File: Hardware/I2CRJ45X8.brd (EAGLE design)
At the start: 76 x 50 mm, 65 parts, among them IC1 MCP23017SO, IC2 MCP23017SO, J1 I2C-BREAKOUT, J2 I2C-BREAKOUT, J3 M01-PLAIN, J4 RJ45-X8

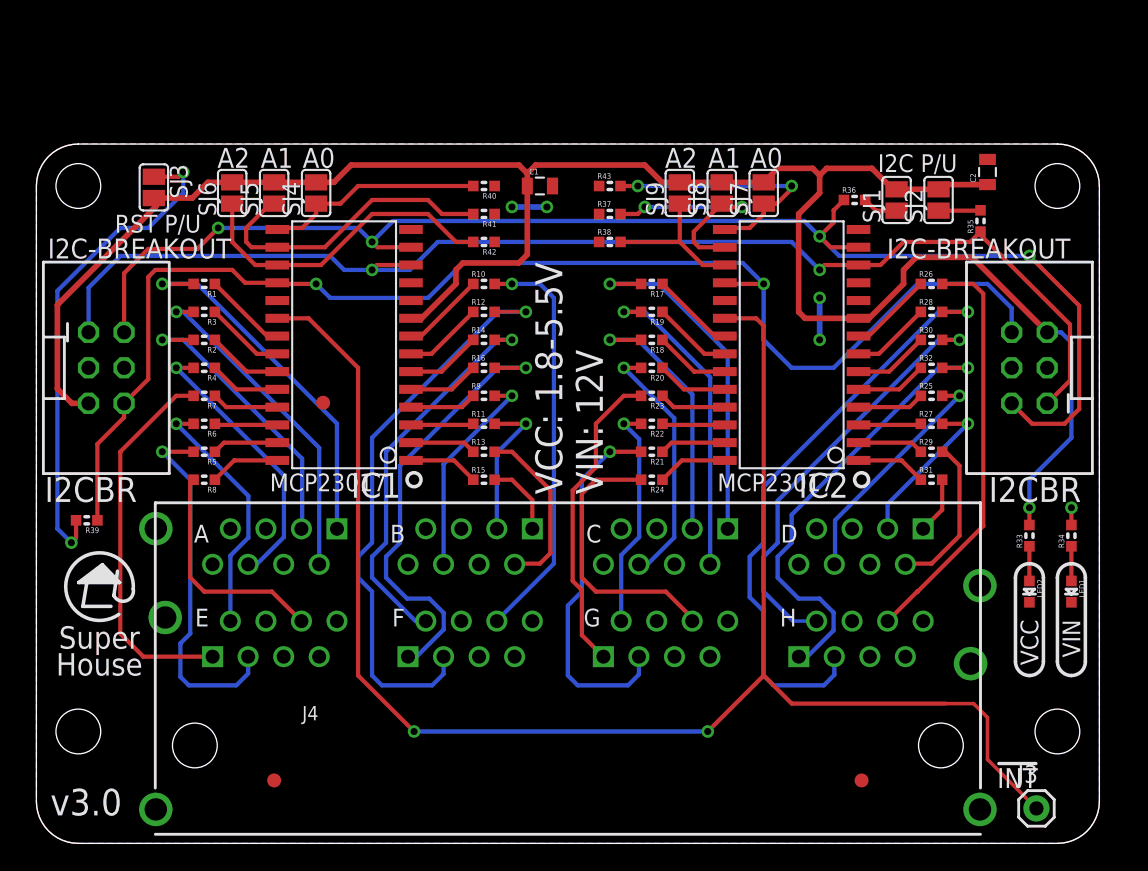
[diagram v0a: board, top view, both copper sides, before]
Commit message: Regenerated 8-port version from updated 16-port version.
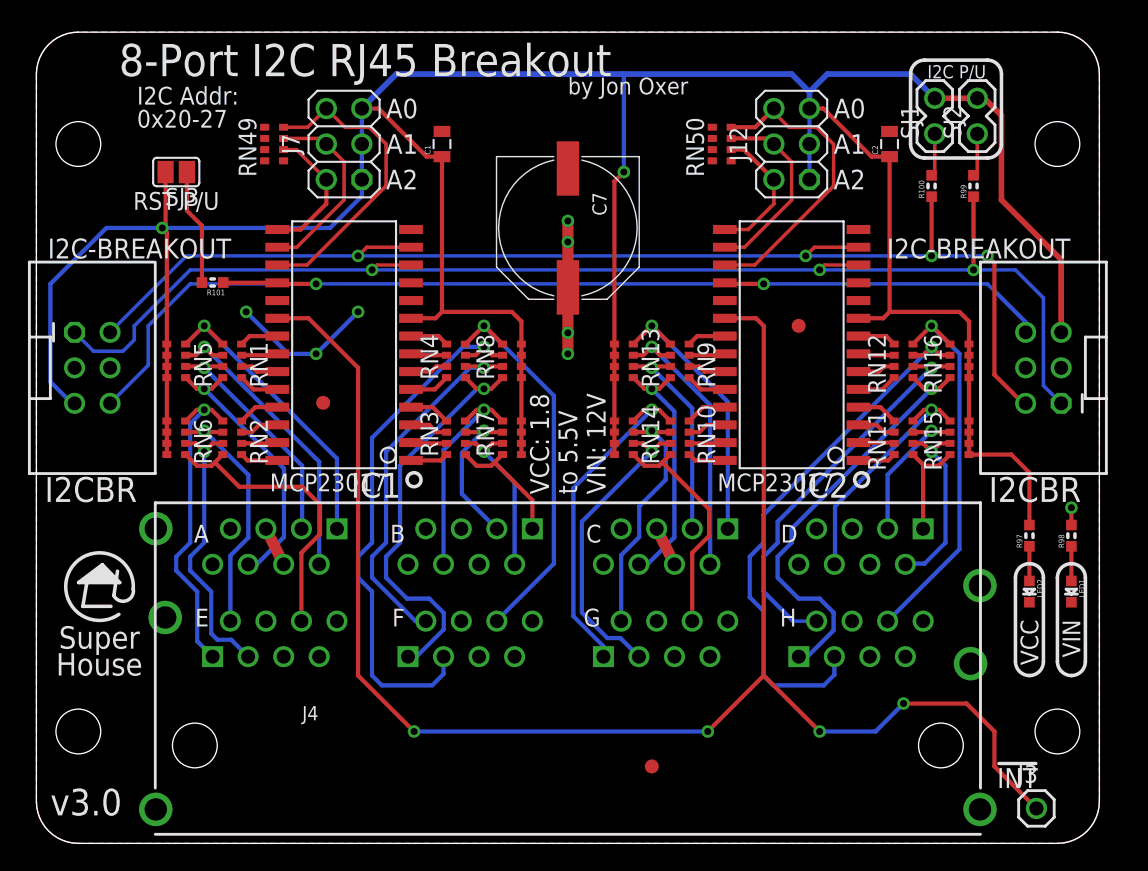
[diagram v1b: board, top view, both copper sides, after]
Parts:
- removed R1, R10, R11, R12, R13, R14, R15, R16, R17, R18, R19, R2, R20, R21, R22, R23, R24, R25, R26, R27, R28, R29, R3, R30, R31, R32, R4, R5, R6, R7, R8, R9: 1K, SuperHouse-DiscreteSemi:R0603
- removed R33, R34, R35, R36: 4K7, SuperHouse-DiscreteSemi:R0603
- removed R37, R38, R39, R40, R41, R42, R43: 10K, SuperHouse-DiscreteSemi:R0603
- removed SJ4, SJ7: A0, SuperHouse-Jumpers:SJ
- removed SJ5, SJ8: A1, SuperHouse-Jumpers:SJ
- removed SJ6, SJ9: A2, SuperHouse-Jumpers:SJ
- added C7: 330uF 50V, SuperHouse-Capacitors:PANASONIC_G
- added J12: I2C Addr 2, SuperHouse-Connectors:2X03-P
- added J7: I2C Addr 1, SuperHouse-Connectors:2X03-P
- added R100, R97, R98, R99: 4K7, SuperHouse-Resistors:R0603
- added R101: 10K, SuperHouse-Resistors:R0603
- added RN1, RN10, RN11, RN12, RN2, RN3, RN4, RN9: 1K, SuperHouse-Resistors:CAY16
- added RN13, RN14, RN15, RN16, RN49, RN5, RN50, RN6, RN7, RN8: 10K, SuperHouse-Resistors:CAY16
- C1, C2: device SuperHouse-DiscreteSemi:C0805 -> SuperHouse-Capacitors:C0805
- J1, J2: device SuperHouse-Connectors:2X03-SHROUDED -> SuperHouse-Connectors:2X3-2.54-SHROUDED
- SJ1, SJ2: device SuperHouse-Jumpers:SJ -> SuperHouse-Connectors:1X02-P
- moved FID2 32.8 mm to (54.5, 37.0)
- moved FID3 27.0 mm to (44.0, 5.50)
- moved C1 7.62 mm to (29.0, 50.0), turned to 90 degrees
- moved C2 7.28 mm to (61.0, 50.0)
- moved SJ2 6.61 mm to (67.3, 52.0)
- moved SJ1 6.59 mm to (64.2, 52.0)
- moved SJ3 1.94 mm to (10.0, 48.0), turned to 180 degrees
- moved J1 1.00 mm to (4.00, 34.0), turned to 270 degrees
- moved J2 1.00 mm to (72.0, 34.0), turned to 90 degrees
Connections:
- net !RESET: now also R101.1; no longer R39.1
- net 1A1: now also RN1.5, RN5.4; no longer R1.2
- net 1A2: now also RN1.6, RN5.3; no longer R3.2
- net 1A3: now also RN1.7, RN5.2; no longer R2.2
- net 1A6: now also RN1.8, RN5.1; no longer R4.2
- net 1B1: now also RN3.5, RN7.4; no longer R15.2
- net 1B2: now also RN3.6, RN7.3; no longer R13.2
- net 1B3: now also RN3.7, RN7.2; no longer R11.2
- net 1B6: now also RN3.8, RN7.1; no longer R9.2
- net 1C1: now also RN13.4, RN9.5; no longer R17.2
- net 1C2: now also RN13.3, RN9.6; no longer R19.2
- net 1C3: now also RN13.2, RN9.7; no longer R18.2
- net 1C6: now also RN13.1, RN9.8; no longer R20.2
- net 1D1: now also RN11.5, RN15.4; no longer R31.2
- net 1D2: now also RN11.6, RN15.3; no longer R29.2
- net 1D3: now also RN11.7, RN15.2; no longer R27.2
- net 1D6: now also RN11.8, RN15.1; no longer R25.2
- net 1E1: now also RN2.5, RN6.4; no longer R7.2
- net 1E2: now also RN2.6, RN6.3; no longer R6.2
- net 1E3: now also RN2.7, RN6.2; no longer R5.2
- net 1E6: now also RN2.8, RN6.1; no longer R8.2
- net 1F1: now also RN4.5, RN8.4; no longer R16.2
- net 1F2: now also RN4.6, RN8.3; no longer R14.2
- net 1F3: now also RN4.7, RN8.2; no longer R12.2
- net 1F6: now also RN4.8, RN8.1; no longer R10.2
- net 1G1: now also RN10.5, RN14.4; no longer R23.2
- net 1G2: now also RN10.6, RN14.3; no longer R22.2
- net 1G3: now also RN10.7, RN14.2; no longer R21.2
- net 1G6: now also RN10.8, RN14.1; no longer R24.2
- net 1H1: now also RN12.5, RN16.4; no longer R32.2
- net 1H2: now also RN12.6, RN16.3; no longer R30.2
- net 1H3: now also RN12.7, RN16.2; no longer R28.2
- net 1H6: now also RN12.8, RN16.1; no longer R26.2
- net GND: now also C7.-, RN49.1, RN49.2, RN49.3, RN49.4, RN50.1, RN50.2, RN50.3, RN50.4; no longer R37.1, R38.1, R40.1, R41.1, R42.1, R43.1
- net GPA0-1: now also RN1.4; no longer R1.1
- net GPA0-2: now also RN9.4; no longer R17.1
- net GPA1-1: now also RN1.3; no longer R3.1
- net GPA1-2: now also RN9.3; no longer R19.1
- net GPA2-1: now also RN1.2; no longer R2.1
- net GPA2-2: now also RN9.2; no longer R18.1
- net GPA3-1: now also RN1.1; no longer R4.1
- net GPA3-2: now also RN9.1; no longer R20.1
- net GPA4-1: now also RN2.4; no longer R7.1
- net GPA4-2: now also RN10.4; no longer R23.1
- net GPA5-1: now also RN2.3; no longer R6.1
- net GPA5-2: now also RN10.3; no longer R22.1
- net GPA6-1: now also RN2.2; no longer R5.1
- net GPA6-2: now also RN10.2; no longer R21.1
- net GPA7-1: now also RN2.1; no longer R8.1
- net GPA7-2: now also RN10.1; no longer R24.1
- net GPB0-1: now also RN3.4; no longer R15.1
- net GPB0-2: now also RN11.4; no longer R31.1
- net GPB1-1: now also RN3.3; no longer R13.1
- net GPB1-2: now also RN11.3; no longer R29.1
- net GPB2-1: now also RN3.2; no longer R11.1
- net GPB2-2: now also RN11.2; no longer R27.1
- net GPB3-1: now also RN3.1; no longer R9.1
- net GPB3-2: now also RN11.1; no longer R25.1
- net GPB4-1: now also RN4.4; no longer R16.1
- net GPB4-2: now also RN12.4; no longer R32.1
- net GPB5-1: now also RN4.3; no longer R14.1
- net GPB5-2: now also RN12.3; no longer R30.1
- net GPB6-1: now also RN4.2; no longer R12.1
- net GPB6-2: now also RN12.2; no longer R28.1
- net GPB7-1: now also RN4.1; no longer R10.1
- net GPB7-2: now also RN12.1; no longer R26.1
- net N$1: now also R99.2; no longer R35.2
- net N$10: now also J12.4, RN50.7; no longer R37.2, SJ8.1
- net N$11: now also IC2.17, J12.6, RN50.8; no longer IC2.15, R43.2, SJ7.1
- net N$2: now also R100.2; no longer R36.2
- net N$3: now also R101.2; no longer R39.2
- net N$4: now also J7.6, RN49.8; no longer R42.2, SJ6.1
- net N$5: now also J7.4, RN49.7; no longer R41.2, SJ5.1
- net N$6: now also J7.2, RN49.6; no longer R40.2, SJ4.1
- net N$7: now also R97.1; no longer R33.1
- net N$8: now also R98.1; no longer R34.1
- net N$9: now also IC2.15, J12.2, RN50.6; no longer IC2.17, R38.2, SJ9.1
- net SCL: now also R99.1; no longer R35.1
- net SDA: now also R100.1; no longer R36.1
- net VCC: now also J12.1, J12.3, J12.5, J7.1, J7.3, J7.5, R97.2, RN13.5, RN13.6, RN13.7, RN13.8, RN14.5, RN14.6, RN14.7, RN14.8, RN15.5, RN15.6, RN15.7, RN15.8, RN16.5, RN16.6, RN16.7, RN16.8, RN5.5, RN5.6, RN5.7, RN5.8, RN6.5, RN6.6, RN6.7, RN6.8, RN7.5, RN7.6, RN7.7, RN7.8, RN8.5, RN8.6, RN8.7, RN8.8; no longer R33.2, SJ4.2, SJ5.2, SJ6.2, SJ7.2, SJ8.2, SJ9.2
- net VIN: now also C7.+, R98.2; no longer R34.2
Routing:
- net VCC: track 148.3 -> 241.9 mm, vias 1 -> 2
- net N$3: track 35.8 -> 8.35 mm, vias 2 -> 0
- net VIN: track 1.24 -> 16.4 mm, vias 1 -> 5
- net !RESET: track 95.9 -> 82.0 mm
- net SDA: track 100.0 -> 89.1 mm
- net N$5: track 21.9 -> 13.9 mm
- net N$6: track 15.7 -> 9.94 mm
- net 1E3: track 26.1 -> 20.5 mm
- net GND: track 5.50 -> 10.5 mm, vias 4 -> 3
- net 1C1: track 25.3 -> 20.5 mm
- net 1E6: track 16.3 -> 21.0 mm
- net 1G3: track 26.4 -> 22.1 mm
- net 1E1: track 27.2 -> 22.9 mm, vias 0 -> 1
- net 1A1: track 26.4 -> 22.2 mm
- net 1C3: track 19.4 -> 15.4 mm
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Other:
- board size 76 x 50 mm -> 76 x 58 mm
- board text added: "I2C Addr: 0x20-27"
- board text added: "VCC: 1.8 to 5.5V VIN: 12V"
- board text removed: "I2C Addr: 0x20 - 0x27"
- board text removed: "VCC: 1.8-5.5V VIN: 12V"
